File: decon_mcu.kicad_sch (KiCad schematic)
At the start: 56 parts, among them J1 Conn_01x02, J10 Conn_01x04, J11 Conn_01x06, J12 Conn_01x06, J13 Conn_01x04, J14 Conn_01x16, J15 Conn_01x16, J16 Conn_01x16, J17 Conn_01x16, J18 Conn_01x04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

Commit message: modified:   DECON_Ctrl_Panel.kicad_pcb 	modified:   DECON_Ctrl_Panel.kicad_prl 	modified:   decon_mcu.kicad_sch
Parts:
- removed J2: GPIO, Connector_PinHeader_2.54mm:PinHeader_1x12_P2.54mm_Vertical, symbol Connector_Generic:Conn_01x12
- added J2: Conn_01x02, Connector_PinHeader_2.54mm:PinHeader_1x02_P2.54mm_Vertical, symbol Connector_Generic:Conn_01x02
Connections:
- net PB5 is gone; now on net MCU_BTN_4: J16.9 (Pin_9), U3.57 (PB5)
- net PB6 is gone; now on net MCU_BTN_3: J16.10 (Pin_10), U3.58 (PB6)
- net PB7 is gone; now on net MCU_BTN_2: J16.11 (Pin_11), U3.59 (PB7)
- net PB8 is gone; now on net MCU_BTN_1: J16.13 (Pin_13), U3.61 (PB8)
- net PB9 is gone; now on net MCU_BTN_0: J16.14 (Pin_14), U3.62 (PB9)
- net PC14 is gone; now on net OSC32_IN: U3.3 (PC14)
- net PC15 is gone; now on net OSC32_OUT: U3.4 (PC15)
- net PH0 is gone; now on net OSC_IN: U3.5 (PH0)
- net PH1 is gone; now on net OSC_OUT: U3.6 (PH1)
- net MCD_D+: now also U3.45 (PA12)
- net MCD_D-: now also U3.44 (PA11)
- net MCU_A0: now also J17.7 (Pin_7), U3.39 (PC8); no longer J14.10 (Pin_10), U3.10 (PC2)
- net MCU_A1: now also J17.6 (Pin_6), U3.38 (PC7); no longer J14.9 (Pin_9), U3.9 (PC1)
- net MCU_A2: now also J17.5 (Pin_5), U3.37 (PC6); no longer J14.8 (Pin_8), U3.8 (PC0)
- net MCU_BTN_0: no longer J17.5 (Pin_5), U3.37 (PC6)
- net MCU_BTN_1: no longer J17.6 (Pin_6), U3.38 (PC7)
- net MCU_BTN_2: no longer J17.7 (Pin_7), U3.39 (PC8)
- net MCU_BTN_3: no longer J17.8 (Pin_8), U3.40 (PC9)
- net MCU_BTN_4: no longer C2.1, J17.9 (Pin_9), R2.2, SW1.1, U3.41 (PA8)
- net PA13: now also U3.46 (PA13)
- net PA14: now also U3.49 (PA14)
- new net PA8: C2.1, J17.9 (Pin_9), J2.1 (Pin_1), R2.2, SW1.1, U3.41 (PA8)
- new net PC0: J14.8 (Pin_8), U3.8 (PC0)
- new net PC1: J14.9 (Pin_9), U3.9 (PC1)
- new net PC2: J14.10 (Pin_10), U3.10 (PC2)
- new net PC9: J17.8 (Pin_8), J2.2 (Pin_2), U3.40 (PC9)

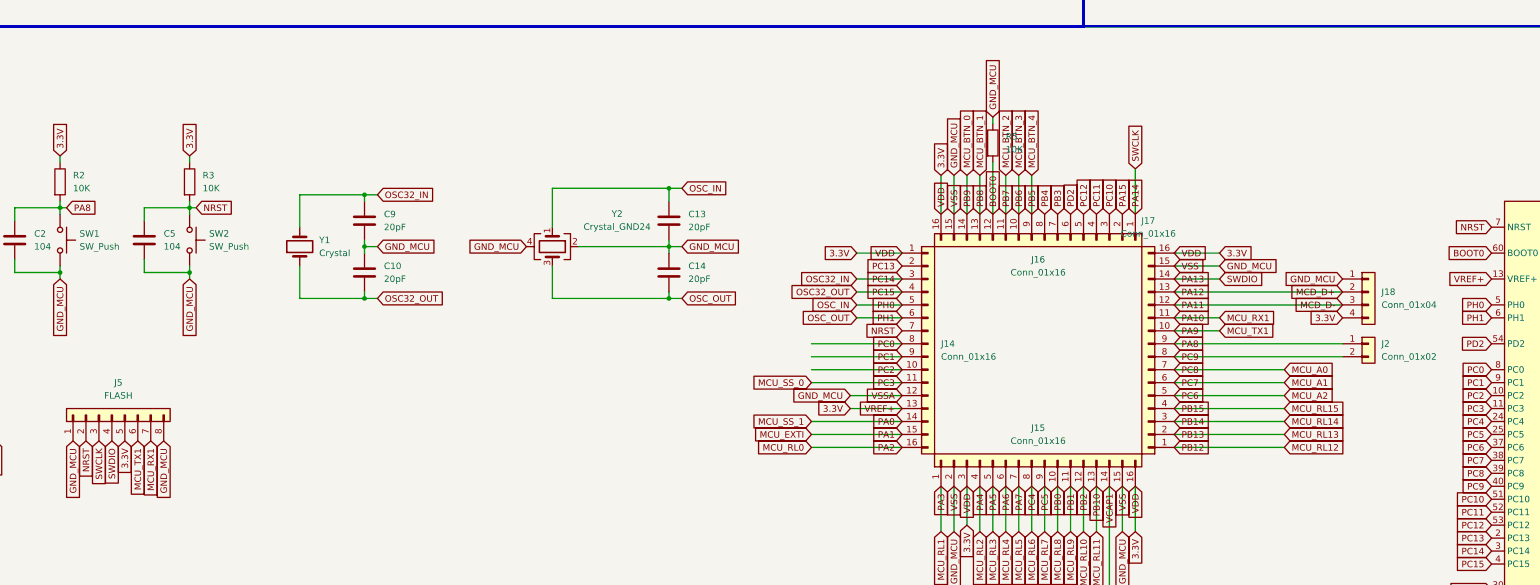
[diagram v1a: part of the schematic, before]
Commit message: modified:   DECON_Ctrl_Panel.kicad_pcb 	modified:   DECON_Ctrl_Panel.kicad_prl 	modified:   button_sensor.kicad_sch 	modified:   decon_mcu.kicad_sch
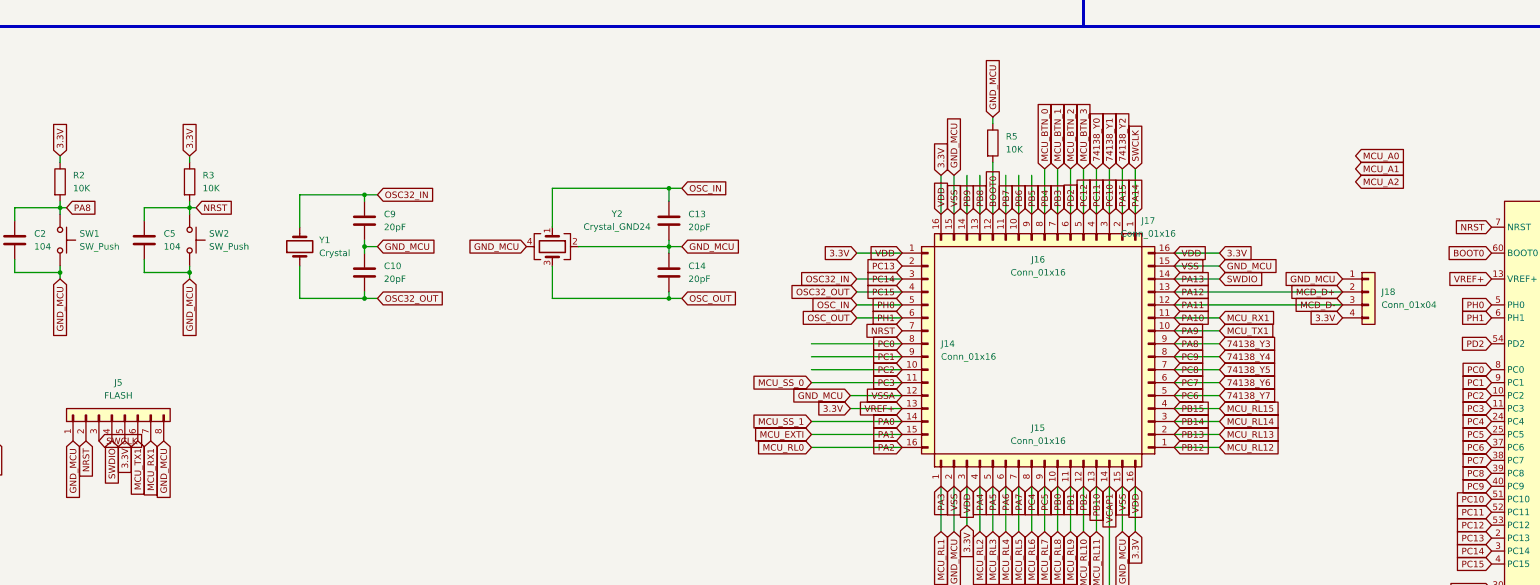
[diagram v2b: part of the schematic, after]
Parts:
- removed J2: Conn_01x02, Connector_PinHeader_2.54mm:PinHeader_1x02_P2.54mm_Vertical, symbol Connector_Generic:Conn_01x02
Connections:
- net PB3 is gone; now on net MCU_BTN_1: J16.7 (Pin_7), U3.55 (PB3)
- net PB4 is gone; now on net MCU_BTN_0: J16.8 (Pin_8), U3.56 (PB4)
- net PC12 is gone; now on net MCU_BTN_3: J16.5 (Pin_5), U3.53 (PC12)
- net PD2 is gone; now on net MCU_BTN_2: J16.6 (Pin_6), U3.54 (PD2)
- net MCU_A0: no longer J17.7 (Pin_7), U3.39 (PC8)
- net MCU_A1: no longer J17.6 (Pin_6), U3.38 (PC7)
- net MCU_A2: no longer J17.5 (Pin_5), U3.37 (PC6)
- net MCU_BTN_0: no longer J16.14 (Pin_14), U3.62 (PB9)
- net MCU_BTN_1: no longer J16.13 (Pin_13), U3.61 (PB8)
- net MCU_BTN_2: no longer J16.11 (Pin_11), U3.59 (PB7)
- net MCU_BTN_3: no longer J16.10 (Pin_10), U3.58 (PB6)
- net MCU_BTN_4 renamed PB5
- net PA15 renamed 74138_Y2
- net PA8 renamed 74138_Y3
- net PC10 renamed 74138_Y1
- net PC11 renamed 74138_Y0
- net PC9 renamed 74138_Y4
- new net 74138_Y5: J17.7 (Pin_7), U3.39 (PC8)
- new net 74138_Y6: J17.6 (Pin_6), U3.38 (PC7)
- new net 74138_Y7: J17.5 (Pin_5), U3.37 (PC6)
- new net PB6: J16.10 (Pin_10), U3.58 (PB6)
- new net PB7: J16.11 (Pin_11), U3.59 (PB7)
- new net PB8: J16.13 (Pin_13), U3.61 (PB8)
- new net PB9: J16.14 (Pin_14), U3.62 (PB9)

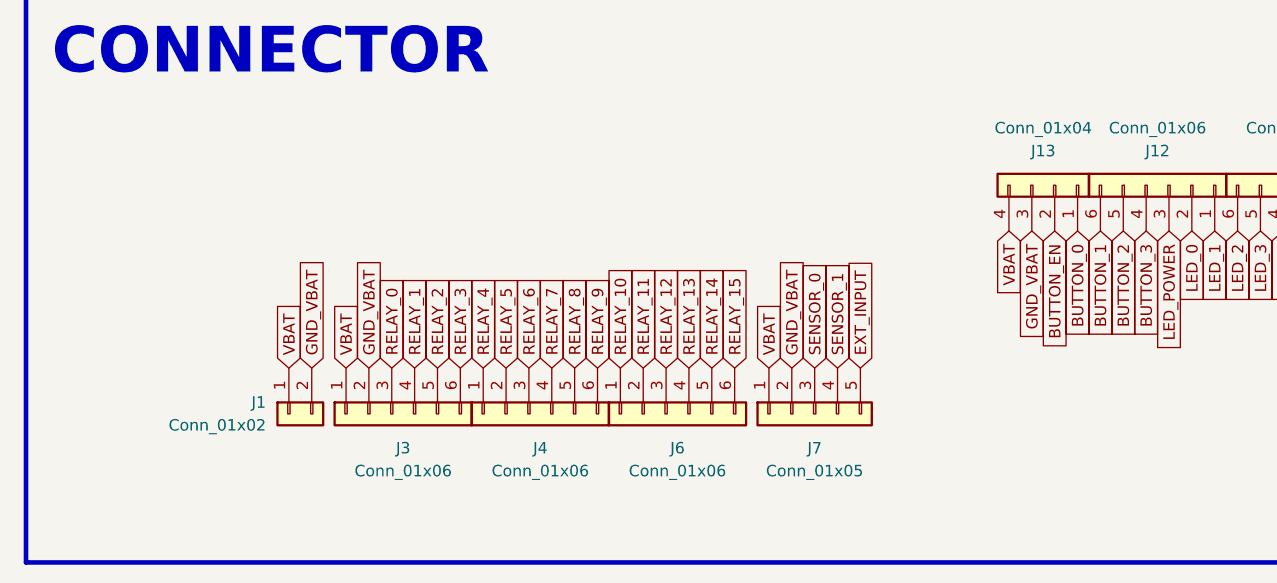
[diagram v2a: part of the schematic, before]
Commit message: modified:   DECON_Ctrl_Panel.kicad_pcb 	modified:   DECON_Ctrl_Panel.kicad_prl 	modified:   decon_mcu.kicad_sch
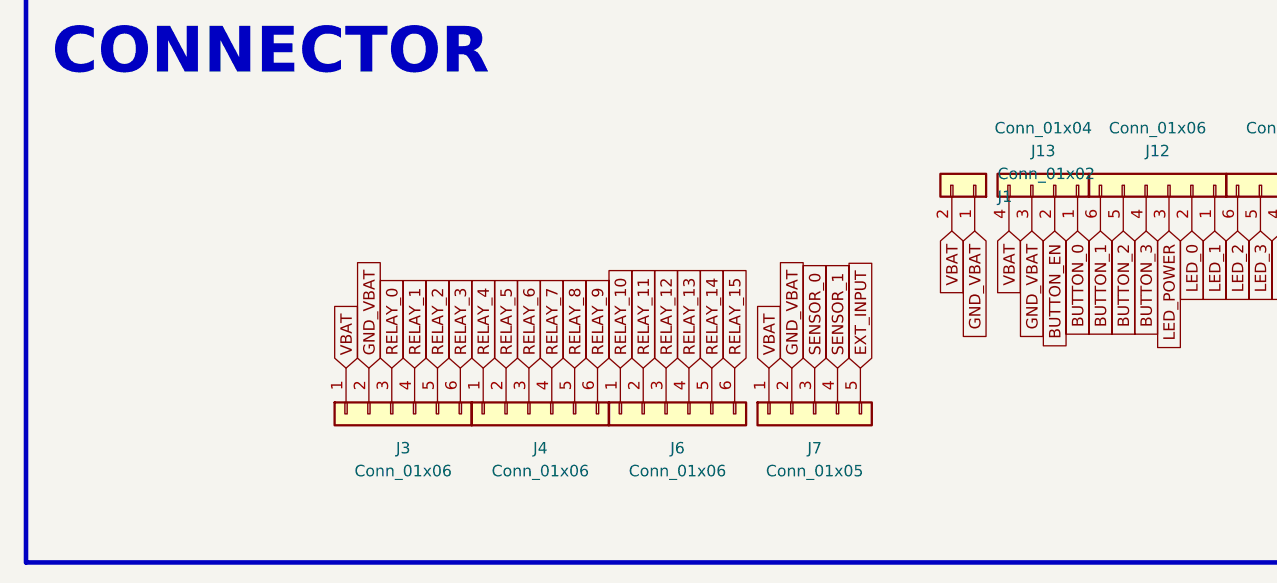
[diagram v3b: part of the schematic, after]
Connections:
- net GND_VBAT: now also J1.1 (Pin_1); no longer J1.2 (Pin_2)
- net VBAT: now also J1.2 (Pin_2); no longer J1.1 (Pin_1)
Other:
- moved on the sheet: J1
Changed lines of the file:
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@@
 		)
 	)
-	(global_label "VBAT"
-		(shape input)
-		(at 44.45 260.35 90)
-		(fields_autoplaced yes)
-		(effects
-			(font
-				(size 1.27 1.27)
-			)
-			(justify left)
-		)
-		(property "Intersheetrefs" "${INTERSHEET_REFS}"
-			(at 44.45 252.95 90)
-			(effects
-				(font
-					(size 1.27 1.27)
-				)
-				(justify left)
-				(hide yes)
-			)
-		)
-	)
 	(global_label "BUTTON_3"
 		(shape input)
@@
 		)
 	)
-	(global_label "GND_VBAT"
-		(shape input)
-		(at 46.99 260.35 90)
-		(fields_autoplaced yes)
-		(effects
-			(font
-				(size 1.27 1.27)
-			)
-			(justify left)
-		)
-		(property "Intersheetrefs" "${INTERSHEET_REFS}"
-			(at 46.99 248.1119 90)
-			(effects
-				(font
-					(size 1.27 1.27)
-				)
-				(justify left)
-				(hide yes)
-			)
-		)
-	)
 	(global_label "BUTTON_1"
 		(shape input)
@@
 		)
 	)
+	(global_label "GND_VBAT"
+		(shape input)
+		(at 120.65 245.11 270)
+		(fields_autoplaced yes)
+		(effects
+			(font
+				(size 1.27 1.27)
+			)
+			(justify right)
+		)
+		(property "Intersheetrefs" "${INTERSHEET_REFS}"
+			(at 120.65 257.3481 90)
+			(effects
+				(font
+					(size 1.27 1.27)
+				)
+				(justify right)
+				(hide yes)
+			)
+		)
+	)
 	(global_label "PB3"
 		(shape input)
@@
 		)
 	)
+	(global_label "VBAT"
+		(shape input)
+		(at 118.11 245.11 270)
+		(fields_autoplaced yes)
+		(effects
+			(font
+				(size 1.27 1.27)
+			)
+			(justify right)
+		)
+		(property "Intersheetrefs" "${INTERSHEET_REFS}"
+			(at 118.11 252.51 90)
+			(effects
+				(font
+					(size 1.27 1.27)
+				)
+				(justify right)
+				(hide yes)
+			)
+		)
+	)
 	(global_label "RELAY_6"
 		(shape input)
@@
 	(symbol
 		(lib_id "Connector_Generic:Conn_01x02")
-		(at 44.45 265.43 90)
+		(at 120.65 240.03 270)
 		(mirror x)
 		(unit 1)
@@
 		(dnp no)
 		(property "Reference" "J1"
-			(at 41.91 264.1599 90)
+			(at 123.19 241.3001 90)
 			(effects
 				(font
@@
 		)
 		(property "Value" "Conn_01x02"
-			(at 41.91 266.6999 90)
+			(at 123.19 238.7601 90)
 			(effects
 				(font
@@
 		)
 		(property "Footprint" "TerminalBlock_MetzConnect:TerminalBlock_MetzConnect_Type086_RT03402HBLC_1x02_P3.81mm_Horizontal"
-			(at 44.45 265.43 0)
+			(at 120.65 240.03 0)
 			(effects
 				(font
@@
 		)
 		(property "Datasheet" "~"
-			(at 44.45 265.43 0)
+			(at 120.65 240.03 0)
 			(effects
 				(font
@@
 		)
 		(property "Description" "Generic connector, single row, 01x02, script generated (kicad-library-utils/schlib/autogen/connector/)"
-			(at 44.45 265.43 0)
+			(at 120.65 240.03 0)
 			(effects
 				(font

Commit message: modified:   DECON_Ctrl_Panel.kicad_pcb 	modified:   DECON_Ctrl_Panel.kicad_prl 	modified:   decon_mcu.kicad_sch 	modified:   fp-info-cache
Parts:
- added D35: LED, LED_SMD:LED_0805_2012Metric, symbol Device:LED
- added J2: Conn_01x06, Connector_PinHeader_2.54mm:PinHeader_1x06_P2.54mm_Vertical, symbol Connector_Generic:Conn_01x06
- added R30: 1K, Resistor_SMD:R_0805_2012Metric, symbol Device:R
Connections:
- net 3.3V: now also R30.1
- net 74138_Y3: no longer C2.1, R2.2, SW1.1
- net PB5: now also J2.6 (Pin_6)
- net PB6: now also J2.5 (Pin_5)
- net PB7: now also J2.4 (Pin_4)
- net PB8: now also J2.3 (Pin_3)
- net PB9: now also J2.2 (Pin_2)
- net PC13: now also J2.1 (Pin_1); no longer D1.1 (K)
- net PC0 renamed BUILTIN_BTN
- net BUILTIN_BTN: now also C2.1, R2.2, SW1.1
- net PC1 renamed BUILTIN_LED_1
- net BUILTIN_LED_1: now also D1.1 (K)
- net PC2 renamed BUILTIN_LED_0
- net BUILTIN_LED_0: now also D35.1 (K)
- new net: D35.2 (A), R30.2

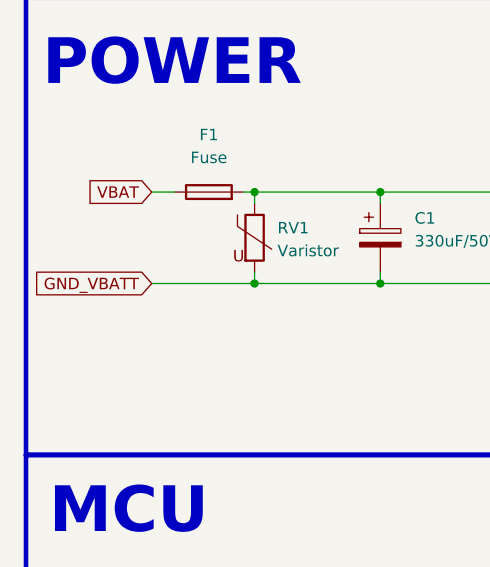
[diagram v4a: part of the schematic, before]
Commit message: modified:   DECON_Ctrl_Panel.kicad_pcb 	modified:   DECON_Ctrl_Panel.kicad_prl 	modified:   decon_mcu.kicad_sch
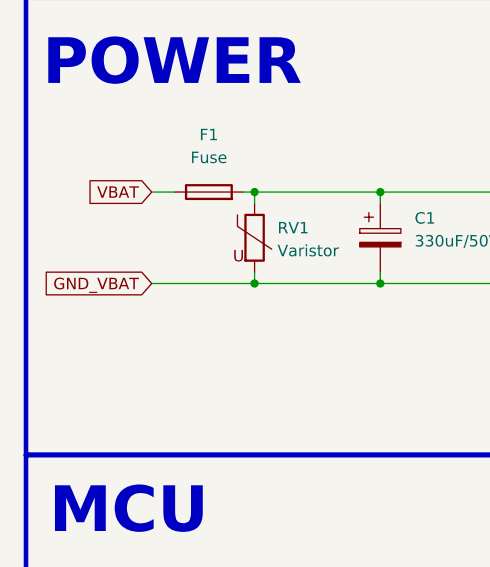
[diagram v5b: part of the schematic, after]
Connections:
- net GND_VBATT is gone; now on net GND_VBAT: C1.2, C3.2, C4.2, C7.1, RV1.2, U1.1 (-VIN)
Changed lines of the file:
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@@
 		)
 	)
-	(global_label "GND_VBATT"
+	(global_label "GND_VBAT"
 		(shape input)
 		(at 29.21 46.99 180)
@@
 		)
 		(property "Intersheetrefs" "${INTERSHEET_REFS}"
-			(at 16.0043 46.99 0)
+			(at 16.9719 46.99 0)
 			(effects
 				(font
